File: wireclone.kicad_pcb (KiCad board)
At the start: 2 copper layers, 98.4 x 48.3 mm, 53 parts, among them P1 CONN_01X03, P2 CONN_01X02, P3 CONN_01X03, P4 CONN_01X02, U1 LME49720, U2 LME49720, U3 LME49600, U4 LME49600, U5 LM7812CT, U6 LM7912CT

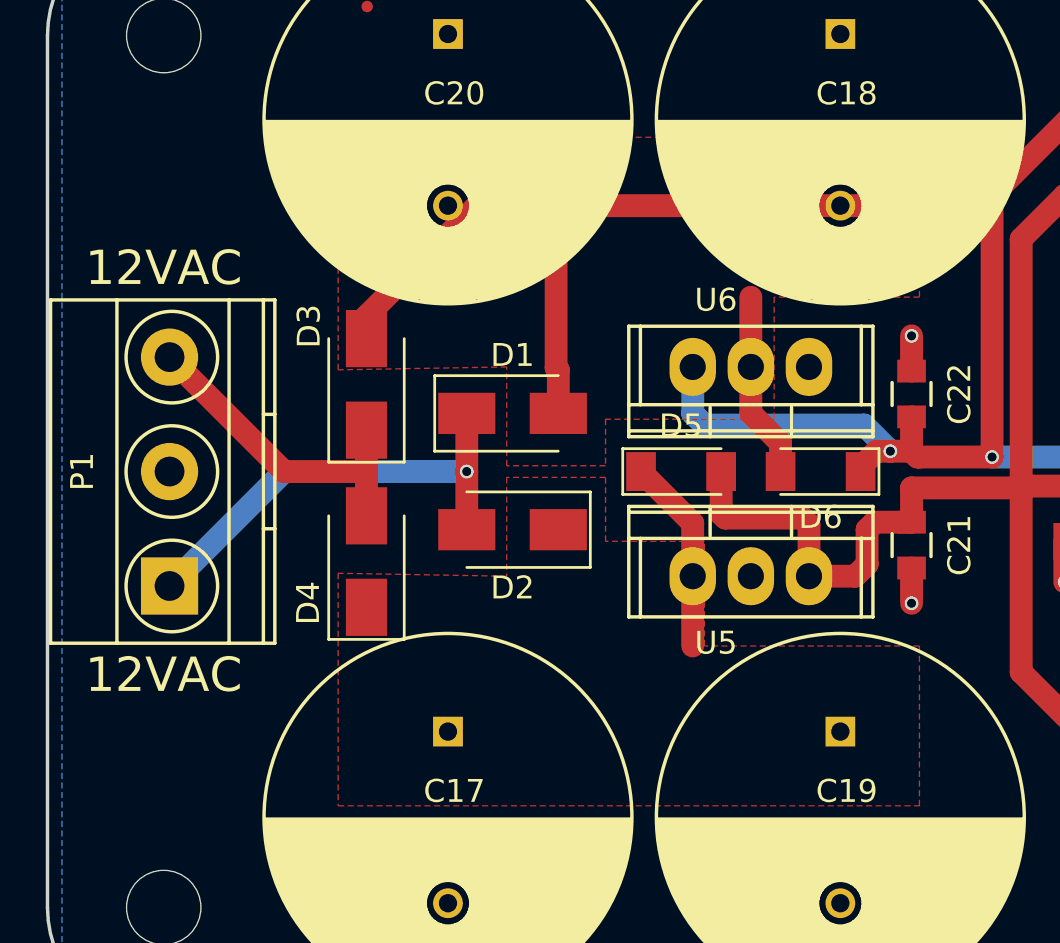
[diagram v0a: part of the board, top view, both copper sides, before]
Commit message: shrunk power connector, made all diodes same type, mentioned 5+5V operation in errata
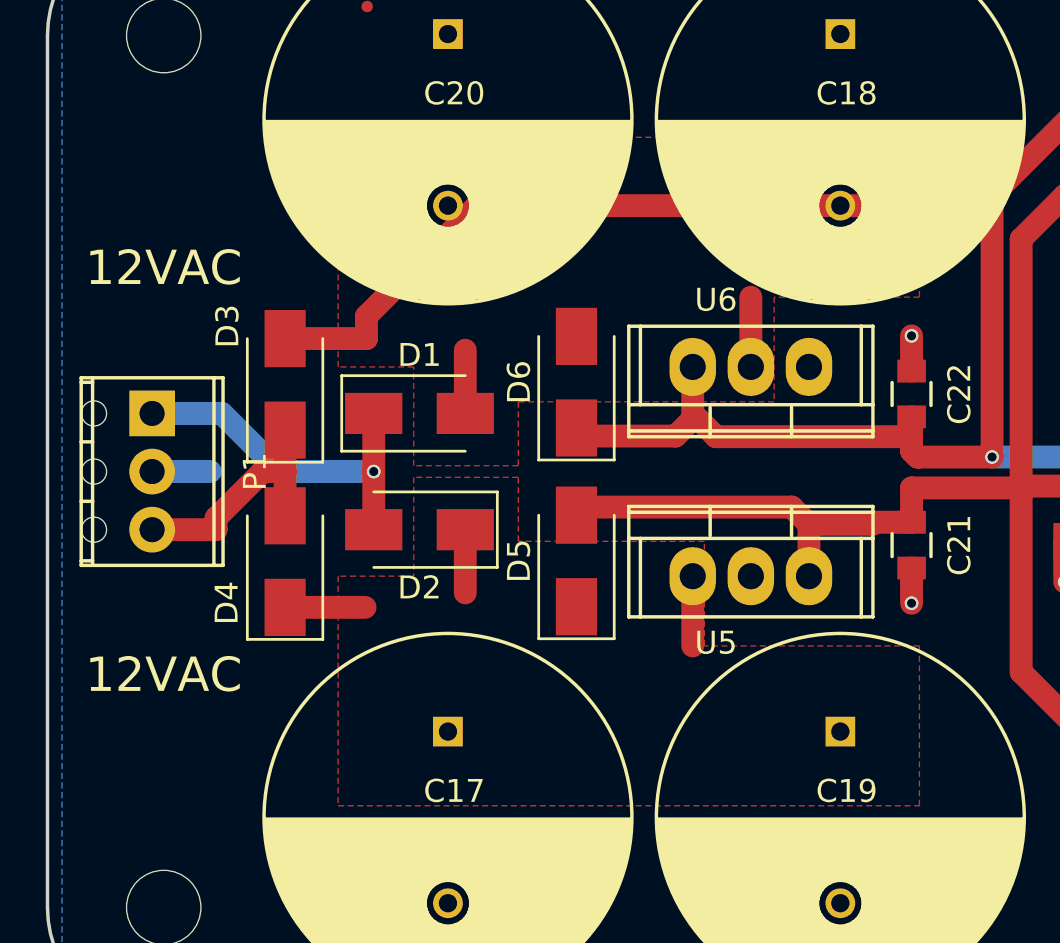
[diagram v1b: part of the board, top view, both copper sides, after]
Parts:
- D5, D6: value LL4148 -> M7; footprint Diodes_SMD:D_MiniMELF -> Diodes_SMD:D_SMA
- P1: footprint Terminal_Blocks:TerminalBlock_Pheonix_MKDS1.5-3pol -> Terminals_Phoenix:TerminalBlock_Phoenix_MPT-2.54mm_3pol
- moved D6 11.4 mm to (80.3, 46.9), turned to 90 degrees
- moved P1 7.58 mm to (61.7, 48.3), turned to 270 degrees
- moved D5 6.01 mm to (80.3, 54.7), turned to 90 degrees
- moved D1 4.06 mm to (73.4, 48.3)
- moved D2 4.06 mm to (73.4, 53.3)
- moved D3 3.56 mm to (67.5, 47.0)
- moved D4 3.56 mm to (67.5, 54.7)
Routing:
- net Net-(C18-Pad2): track 42.2 -> 34.3 mm
- net /PSU/AC2: track 20.1 -> 15.8 mm
- net /PSU/AC1: track 14.4 -> 10.9 mm
- net /PSU/VEE: track 462.2 -> 465.4 mm, vias 94 -> 93
- net GND: track 59.4 -> 62.0 mm
- net /PSU/VCC: track 124.4 -> 126.9 mm
- net Net-(C17-Pad1): track 8.56 -> 9.31 mm
